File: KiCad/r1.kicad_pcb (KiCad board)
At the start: 2 copper layers, 215.9 x 127 mm, 77 parts, among them J1 KEYBOARD, J2 VIDEO OUT, J3 ATX-20, J4 DE9_Socket, J5 R1 EXPANSION, J7 7-9V DC, Q1 2N4401, U1 6502, U10 74LS245, U11 MAX232, U2 6821, U3 27C64, U4 HM62256BLP, U5 74LS138, U6 74LS00, U7 74LS04, U8 P8X32A-D40, U9 24LC256, X1 1 MHz, X2 5MHz

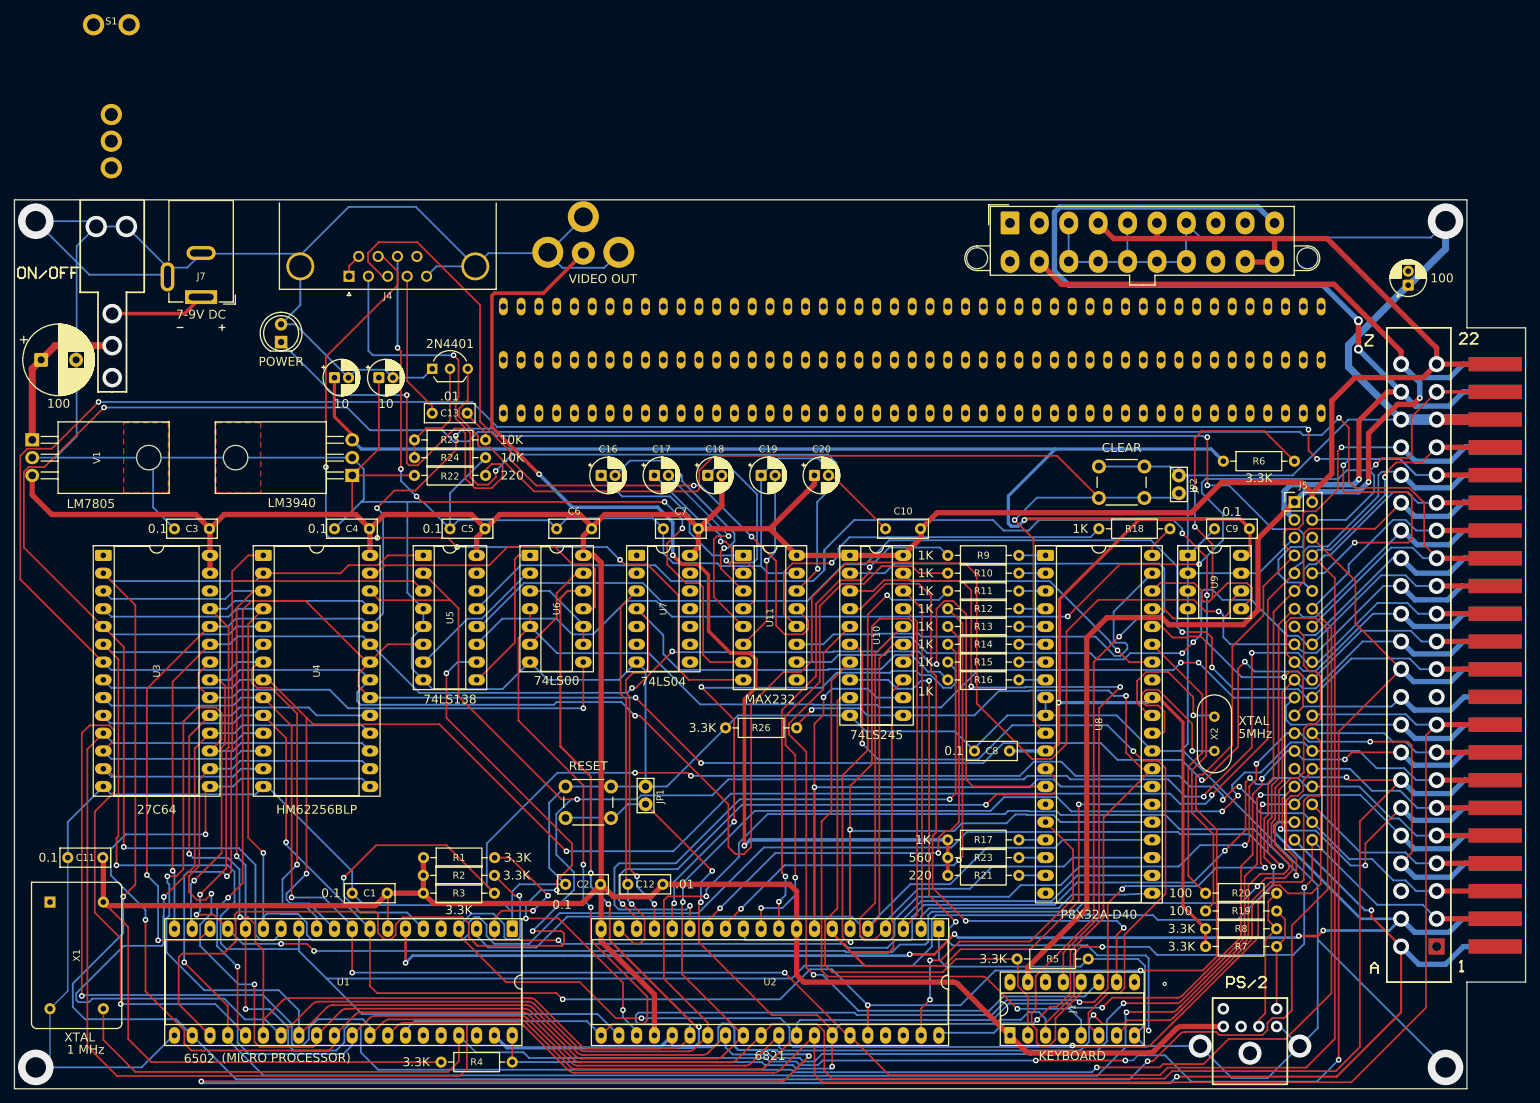
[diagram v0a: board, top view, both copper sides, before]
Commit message: Create edge finger footprints and trace cleanup
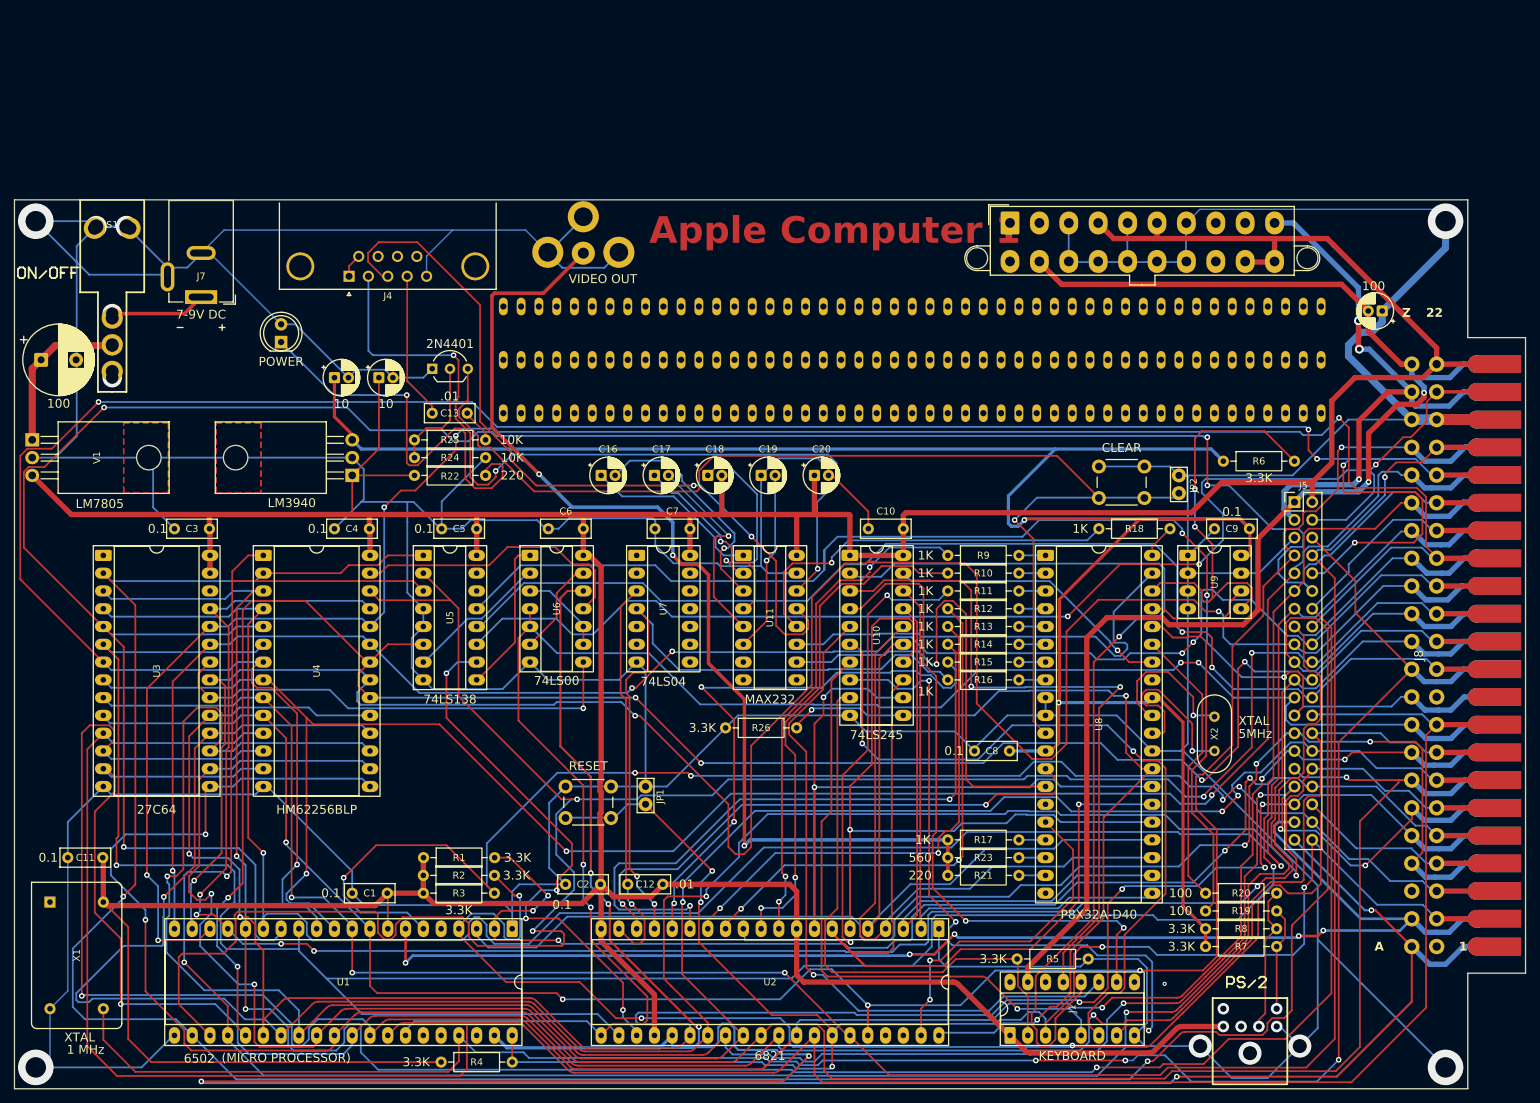
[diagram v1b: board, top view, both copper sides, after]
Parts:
- added J8: Conn_02x22_Counter_Clockwise, r1te:CardEdgeConnector_44p_P156mils, F.Cu at (254.0, -96.5)
- added REF**: A1EdgeFingers, r1te:A1EdgeFingers, F.Cu at (259.7, -96.5)
- moved S1 29.1 mm to (64.8, -199.1)
- moved C22 5.23 mm to (246.2, -187.3), turned to 180 degrees
- moved C10 2.46 mm to (172.8, -156.2)
- moved C6 1.19 mm to (127.1, -156.2)
- moved C5 1.19 mm to (111.8, -156.2)
- moved C7 1.19 mm to (142.3, -156.2)
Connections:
- J7 pad 3: GND -> (no net)
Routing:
- net unconnected-(U11-R2IN-Pad8): track 119.9 -> 0.00 mm, vias 4 -> 0
- net unconnected-(U11-T2OUT-Pad7): track 104.4 -> 0.00 mm, vias 5 -> 0
- net +12V: track 147.4 -> 82.9 mm, vias 4 -> 3
- net (no net): track 13.5 -> 0.00 mm, vias 9 -> 4
- net GND: track 1130.2 -> 1140.0 mm
- net /A4: track 382.8 -> 377.6 mm, vias 3 -> 2
- net Net-(J2-In): track 155.7 -> 152.1 mm
- net VCC: track 726.1 -> 729.5 mm, vias 2 -> 1
- net /A6: track 312.3 -> 309.8 mm, vias 3 -> 2
- net /SYNC: track 192.4 -> 194.0 mm, vias 6 -> 5
- net /$C000: track 190.3 -> 188.8 mm, vias 4 -> 3
- net /A10: track 329.9 -> 328.5 mm, vias 4 -> 3
- net /$A000: track 185.5 -> 184.3 mm, vias 4 -> 3
- net Net-(U4-~{WE}): track 42.2 -> 41.2 mm
- net /A3: track 373.8 -> 372.9 mm, vias 7 -> 6
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- added copper zone on B.Cu, net GND
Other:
- board size 215.9 x 127 mm -> 207.6 x 127 mm
- board text added: "Apple Computer 1"
